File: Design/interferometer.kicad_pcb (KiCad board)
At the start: 4 copper layers, 56.9 x 53.3 mm, 43 parts, among them J1 GS2, Q1 FDC637BNZ, U1 ADN8810ACPZ, U2 OPA320SAIDBVT, U3 ADR292GRUZ

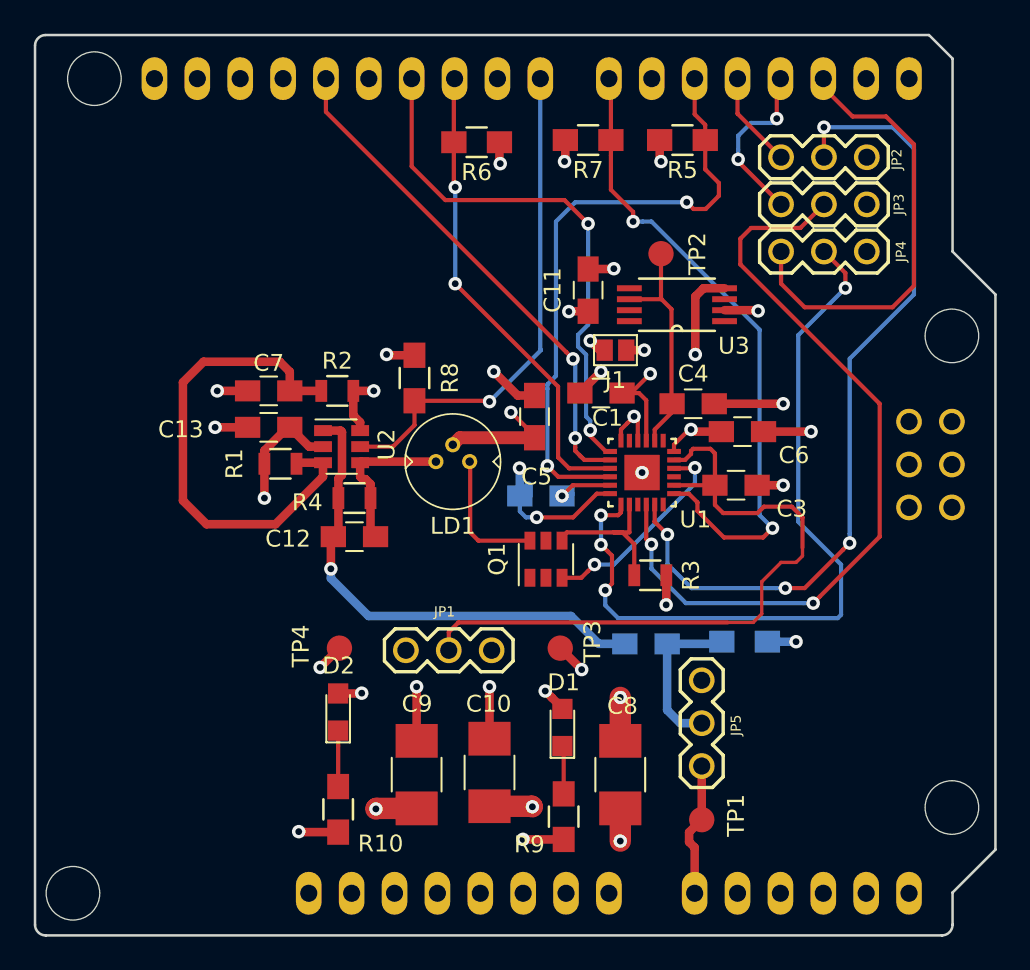
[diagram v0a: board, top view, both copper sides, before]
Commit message: modify design for manufacturing
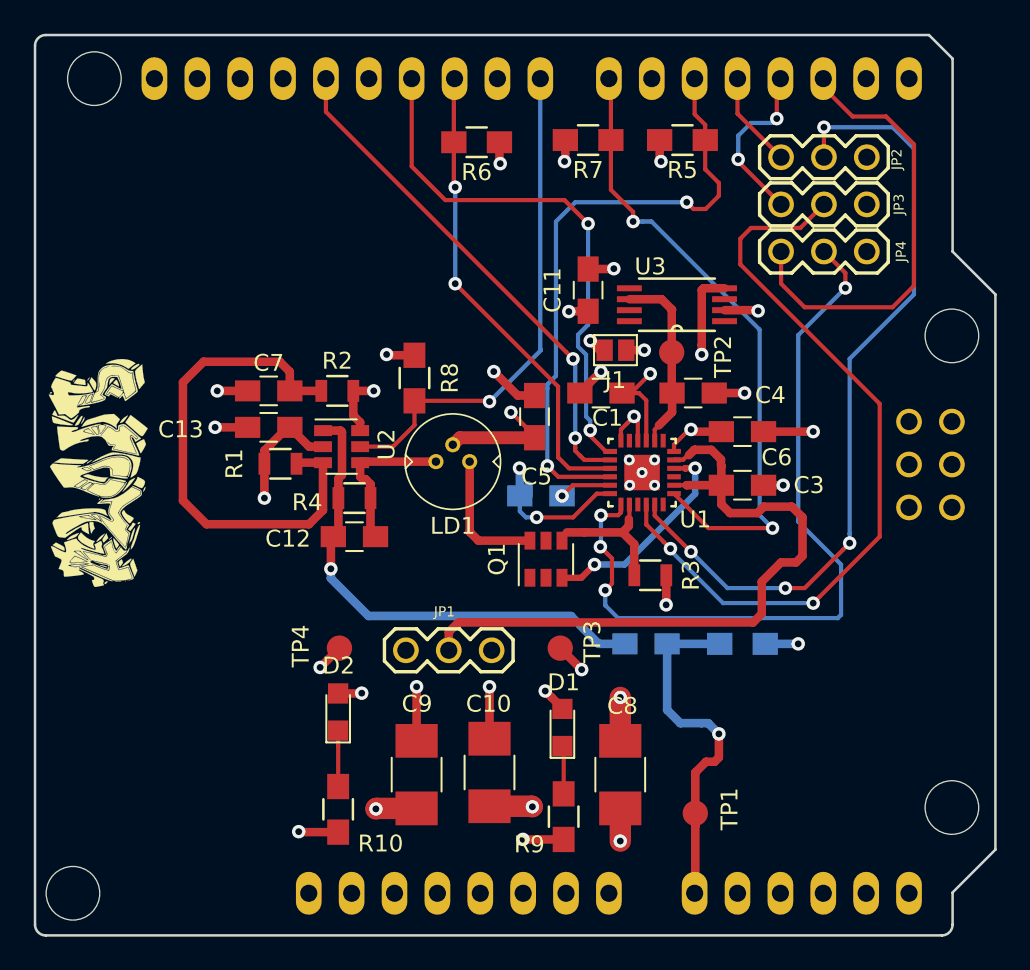
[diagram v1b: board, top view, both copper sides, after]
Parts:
- removed JP5: Jumper_NC_Dual, freetronics_footprints:1X03
- added G***: LOGO, footprints:Alois_name_logo, F.Cu at (131.7, 97.2)
- moved TP2 5.88 mm to (165.6, 90.0)
- moved C4 0.63 mm to (166.9, 92.5)
- moved TP1 0.54 mm to (167.0, 117.3)
- moved C3 0.38 mm to (169.8, 97.9)
- moved R11 0.18 mm to (169.8, 107.3)
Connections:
- C14 pad 1: Net-(C14-Pad1) -> /A0
- R11 pad 1: Net-(C14-Pad1) -> /A0
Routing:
- net Net-(C3-Pad1): track 41.5 -> 59.4 mm
- net /A0: track 7.98 -> 21.2 mm, vias 0 -> 1
- net Net-(C14-Pad1): track 9.59 -> 0.00 mm
- net /LD: track 7.80 -> 12.0 mm
- net /4.096_VREF: track 13.7 -> 11.0 mm
- net Earth: track 42.2 -> 39.9 mm
- net /chip_addr1: track 46.8 -> 45.5 mm
- net /chip_addr0: track 48.9 -> 47.7 mm
- net Net-(C7-Pad2): track 29.8 -> 30.9 mm
- net /AVSS: track 25.6 -> 26.7 mm, vias 8 -> 12
- net /~laser_standby: track 38.7 -> 38.0 mm
- net /RSN: track 9.30 -> 8.55 mm
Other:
- net class current_control added: clearance 0.2, trace_width 0.381, via_dia 0.8, via_drill 0.4
- net class vias_gndplane added: clearance 0.2, trace_width 0.25, via_dia 0.65, via_drill 0.3
